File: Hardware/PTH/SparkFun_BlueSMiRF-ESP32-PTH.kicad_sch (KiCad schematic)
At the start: 27 parts, among them J2 Conn_01x06, Q1 Q_NMOS_DGS, Q2 Q_NMOS_DGS, SW1 Switch, U1 ESP32_Pico_Mini, U2 AP2112K-3.3

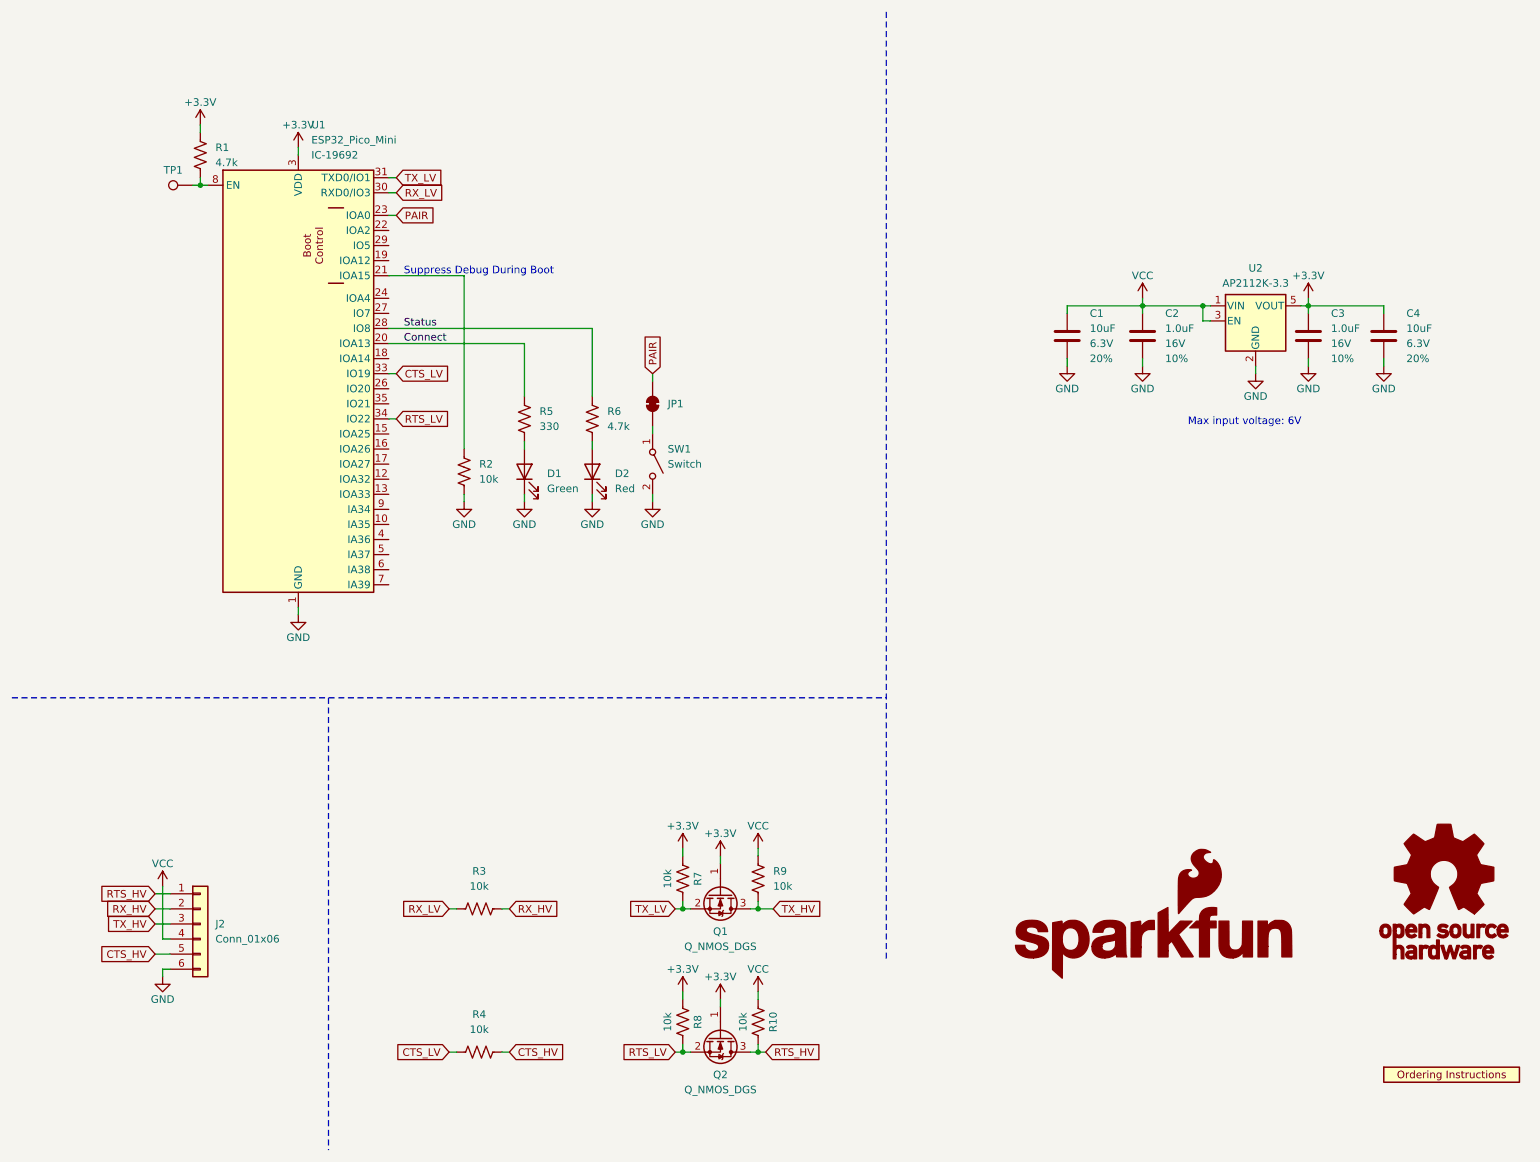
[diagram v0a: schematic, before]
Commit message: Post design review fixes.
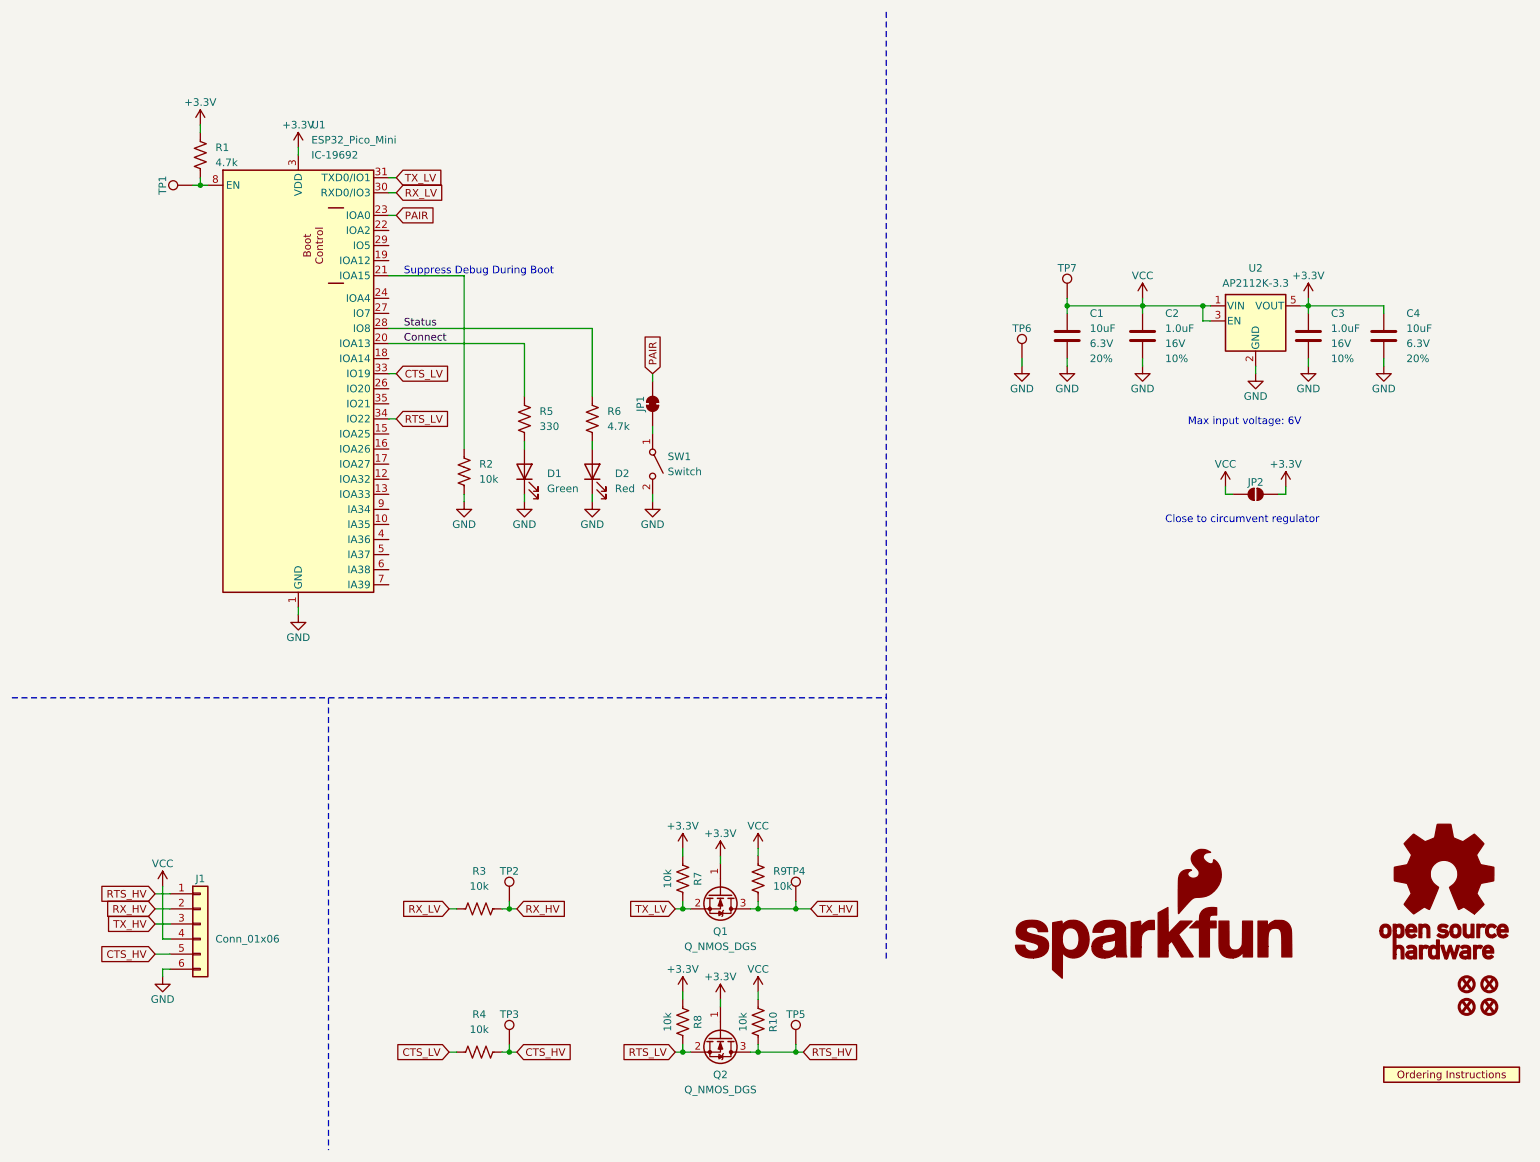
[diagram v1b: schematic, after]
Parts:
- added FID1, FID2, FID3, FID4: Fiducial_0.5, SparkFun-Aesthetic:Fiducial_0.5mm_Mask1mm, symbol SparkFun-Aesthetic:Fiducial_0.5
- added JP2: ~, SparkFun-Jumper:SMT-JUMPER_2_NO_SILK, symbol SparkFun-Jumper:SolderJumper_2_Open
- added TP2, TP3, TP4, TP5, TP6, TP7: TestPoint_0.75mm, SparkFun-Connector:TestPoint-0.75mm, symbol SparkFun-Connector:TestPoint_0.75mm
- renumbered J2 to J1
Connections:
- net +3.3V: now also JP2.2 (B)
- net CTS_HV: now also TP3.1
- net GND: now also TP6.1
- net RTS_HV: now also TP5.1
- net RX_HV: now also TP2.1
- net TX_HV: now also TP4.1
- net VCC: now also JP2.1 (A), TP7.1
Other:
- note added: "Close to circumvent regulator"

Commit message: Apply design review changes to PTH version.
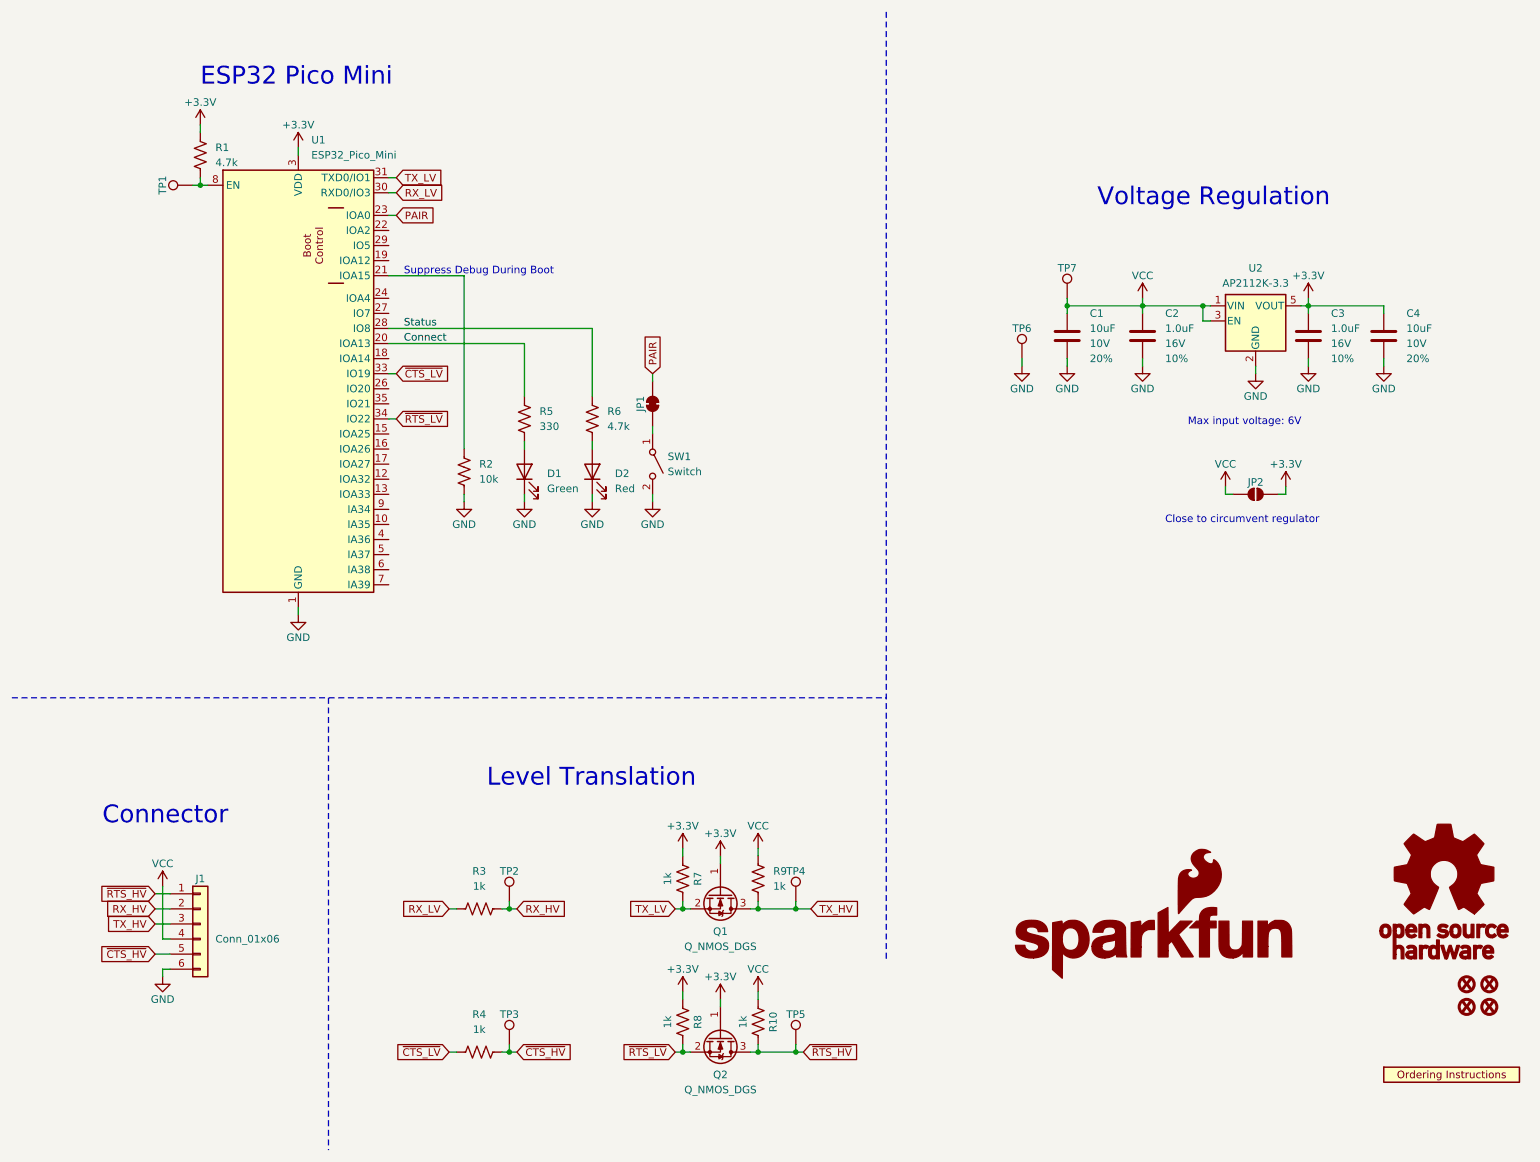
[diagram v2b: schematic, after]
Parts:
- C1, C4: symbol SparkFun-Capacitor:10uF_0603_6.3V_20% -> SparkFun-Capacitor:10uF_0603_10V_20%; PROD_ID CAP-11015 -> CAP-20155; Voltage 6.3V -> 10V
- R10, R3, R4, R7, R8, R9: value 10k -> 1k; symbol SparkFun-Resistor:10k_0603 -> SparkFun-Resistor:1k_0603; PROD_ID RES-00824 -> RES-07856
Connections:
- net CTS_HV renamed ~{CTS_HV}
- net CTS_LV renamed ~{CTS_LV}
- net RTS_HV renamed ~{RTS_HV}
- net RTS_LV renamed ~{RTS_LV}
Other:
- note added: "Connector"
- note added: "ESP32 Pico Mini"
- note added: "Level Translation"
- note added: "Voltage Regulation"
- title: BlueSMiRF - ESP32 -> SparkFun BlueSMiRF - ESP32 PTH

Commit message: Change BSS138 resistors to 10k
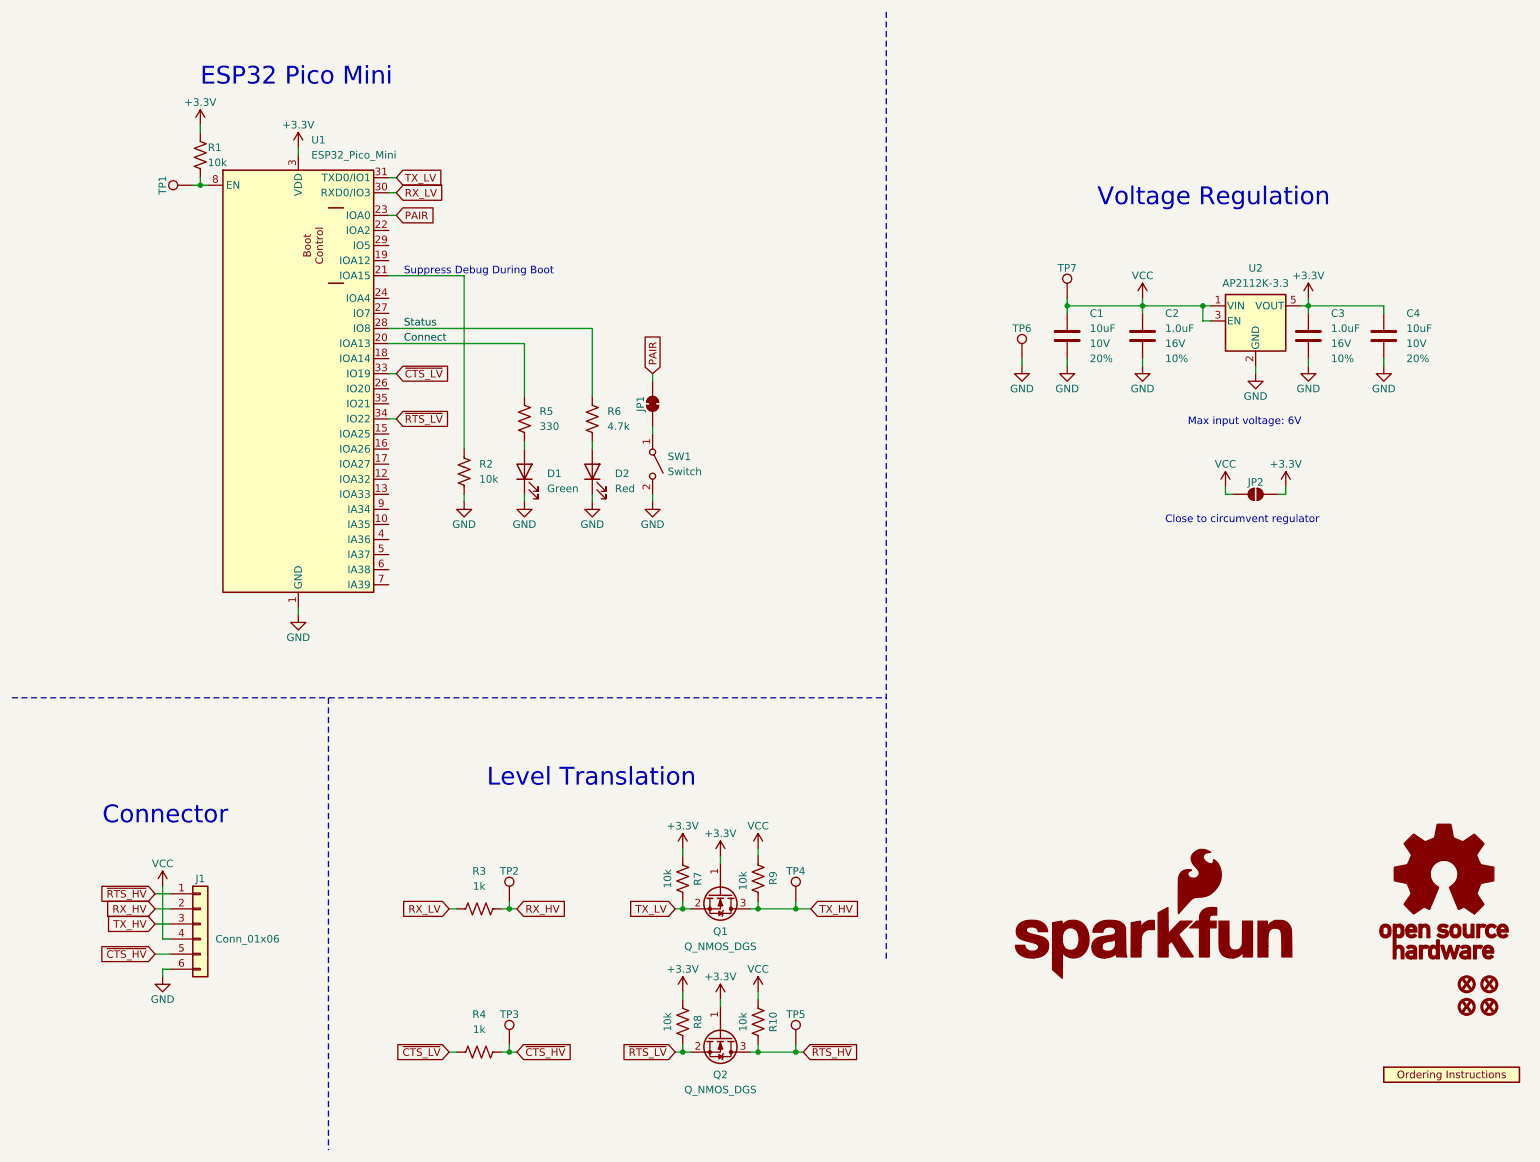
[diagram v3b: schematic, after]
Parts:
- R1: value 4.7k -> 10k; symbol SparkFun-Resistor:4.7k_0603 -> SparkFun-Resistor:10k_0603; PROD_ID RES-07857 -> RES-00824
- R10, R7, R8, R9: value 1k -> 10k; symbol SparkFun-Resistor:1k_0603 -> SparkFun-Resistor:10k_0603; PROD_ID RES-07856 -> RES-00824
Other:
- moved on the sheet: R1, R10, R7, R8, R9
